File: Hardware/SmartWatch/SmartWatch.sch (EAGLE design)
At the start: 70 parts, among them U1 STM32L476, U3 UG-2828GDEDF11, U4 FAN5331SX, U5 APDS-9960, U6 MCP73831, U7 AP2112K-3.3TRG-1

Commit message: finished schematic!
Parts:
- added R19, R22: 10k, resistor:R-US_R0603
- added R21: 10K, resistor:R-US_R0603
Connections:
- removed net BT_IRQ: U2.P0.25
- removed net MOSI/DATA1: U3.D1/SDIN
- removed net PA10: U1PORTA.P10
- removed net PA13: U1PORTA.P13
- removed net PA5: U1PORTA.P5
- removed net PA6: U1PORTA.P6
- removed net PA7: U1PORTA.P7
- removed net PA8: U1PORTA.P8
- removed net PB0: U1PORTB.P0
- removed net PB1: U1PORTB.P1
- removed net PB13: U1PORTB.P13
- removed net PB14: U1PORTB.P14
- removed net PB2: U1PORTB.P2
- removed net PB8: U1PORTB.P8
- removed net PB9: U1PORTB.P9
- removed net PC10: U1PORTC.P10
- removed net PC12: U1PORTC.P12
- removed net PC4: U1PORTC.P4
- removed net PC8: U1PORTC.P8
- removed net PC9: U1PORTC.P9
- removed net SCK/DATA0: U3.D0/SCK
- new net BT_INT: U1PORTC.P4, U2.P0.25
- new net OLED_MOSI: U1PORTC.P12, U3.D1/SDIN
- new net OLED_SCK: U1PORTC.P10, U3.D0/SCK
- net 3.3V: now also R21.2
- net BTN_BACK: now also U1PORTA.P10
- net BTN_DN: now also U1PORTB.P0
- net BTN_SEL: now also U1PORTB.P1
- net BTN_UP: now also U1PORTB.P2
- net BT_MISO: now also U1PORTA.P6
- net BT_MOSI: now also U1PORTA.P7
- net BT_SCK: now also U1PORTA.P5
- net GND: now also R19.1, R22.1
- net G_INT: now also U1PORTC.P8
- net IMU_INT: now also U1PORTC.P9
- net IMU_NRESET: now also R22.2, U1PORTA.P8
- net OLED_CS: now also R19.2
- net OLED_DC: now also U1PORTB.P9
- net OLED_RES: now also U1PORTB.P8
- net SCL: now also U1PORTB.P13
- net SDA: now also U1PORTB.P14
- net STAT: now also R21.1, U1PORTA.P13
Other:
- moved on the sheet: R11, R12, R2

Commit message: started board layout
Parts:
- added JP1: (no value), SparkFun-Connectors:M02PTH
- C1, C10, C11, C14, C2, C3, C4, C5, C6, C7, C8, C9: device microbuilder:CAP_CERAMIC0603MINI -> resistor:C-EUC0603
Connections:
- removed net 3.3V: BTN_BACK.34, BTN_BOOT0.34, BTN_DN.34, BTN_NRST.34, BTN_SEL.34, BTN_UP.34, C10.2, C11.2, C12.1, C13.1, C18.1, C19.1, C20.1, C21.1, C22.1, C23.1, C24.1, C25.1, C26.1, C29.1, C3.2, C5.2, C7.1, C9.2, L1.1, R21.2, R3.2, R8.2, R9.2, U$39.VCC, U$41.VCC, U$5.NBOOT, U$5.VDD, U$5.VDDIO, U1G$4.VBAT, U1G$4.VDD, U1G$4.VDD/PF5, U1G$4.VDD/VUSB, U1G$4.VDD1, U1G$4.VDDA/VREF+, U3.VCI, U3.VDDIO, U4.SHDN, U4.VIN, U5.LEDA, U5.VDD, U7.VCC
- net +3V3: now also BTN_BACK.34, BTN_BOOT0.34, BTN_DN.34, BTN_NRST.34, BTN_SEL.34, BTN_UP.34, C10.2, C11.2, C12.1, C13.1, C18.1, C19.1, C20.1, C21.1, C22.1, C23.1, C24.1, C25.1, C26.1, C29.1, C3.2, C5.2, C7.1, C9.2, L1.1, R21.2, R3.2, R8.2, R9.2, U$39.VCC, U$41.VCC, U$5.NBOOT, U$5.VDD, U$5.VDDIO, U1G$4.VBAT, U1G$4.VDD, U1G$4.VDD/PF5, U1G$4.VDD/VUSB, U1G$4.VDD1, U1G$4.VDDA/VREF+, U3.VCI, U3.VDDIO, U4.SHDN, U4.VIN, U5.LEDA, U5.VDD, U7.VCC
- net GND: now also JP1.1
- net VBAT: now also JP1.2
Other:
- moved on the sheet: C1, C10, C11, C4, C5, C7, C8

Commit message: updated with ext programming port also eliminated some gnd loops and added text
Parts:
- added JP2: (no value), SparkFun-Connectors:M04NO_SILK_ALL_ROUND
- C10: value 1.0uF -> 1uF
- C2, C6: value 10uF/16V -> 10uF
- C22: value 0.1nF -> 0.1uF
- R13, R14, R15, R16, R17, R18, R20, R21, R7, R9: value 10K -> 10k
- R4: value 600K -> 600k
- R6: value 100K -> 100k
- RN1: value (none) -> 22
- renumbered U$16 to U10, U$39 to U9, U$41 to U8, U$5 to U11
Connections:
- removed net PA9: U1PORTA.P9
- removed net PC14: U1PORTC.P14
- new net SWCLK: JP2.4, U1PORTA.P14
- new net SWDIO: JP2.3, U1PORTA.P13
- net +3V3: now also JP2.1
- net GND: now also JP2.2
- net OSC32_IN: now also U1PORTC.P14; no longer U1PORTA.P14
- net STAT: now also U1PORTA.P9; no longer U1PORTA.P13

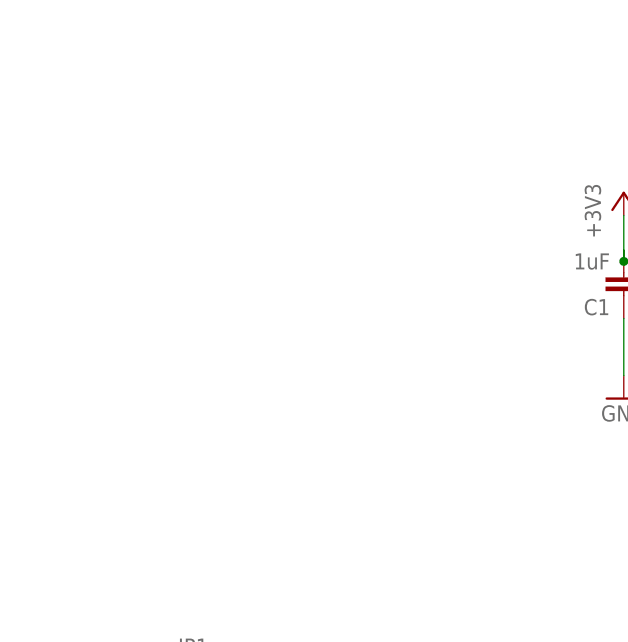
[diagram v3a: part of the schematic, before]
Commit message: added mounting holes
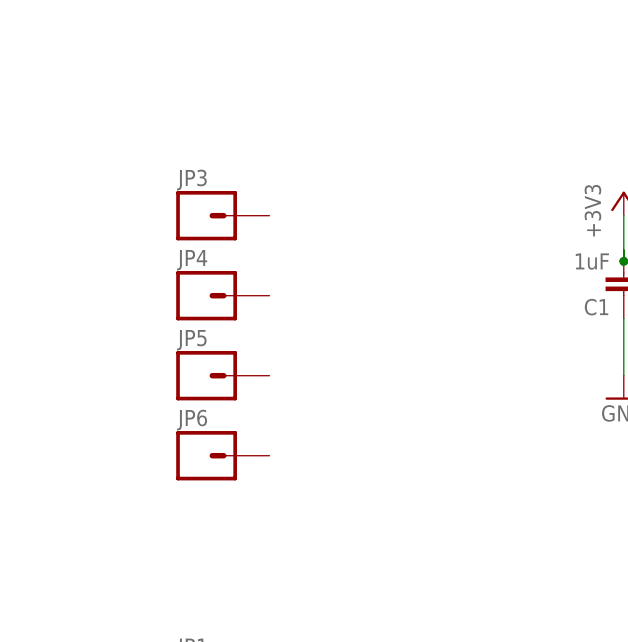
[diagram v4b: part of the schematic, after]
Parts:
- added JP3, JP4, JP5, JP6: (no value), SparkFun-Connectors:M01PTH_NO_SILK_YES_STOP
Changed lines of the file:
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@@
 <part name="JP1" library="SparkFun-Connectors" deviceset="M02" device="PTH"/>
 <part name="JP2" library="SparkFun-Connectors" deviceset="M04" device="NO_SILK_ALL_ROUND"/>
+<part name="JP3" library="SparkFun-Connectors" deviceset="M01" device="PTH_NO_SILK_YES_STOP"/>
+<part name="JP4" library="SparkFun-Connectors" deviceset="M01" device="PTH_NO_SILK_YES_STOP"/>
+<part name="JP5" library="SparkFun-Connectors" deviceset="M01" device="PTH_NO_SILK_YES_STOP"/>
+<part name="JP6" library="SparkFun-Connectors" deviceset="M01" device="PTH_NO_SILK_YES_STOP"/>
 </parts>
 <sheets>
@@
 <instance part="JP1" gate="G$1" x="-33.02" y="24.13"/>
 <instance part="JP2" gate="G$1" x="107.95" y="7.62"/>
+<instance part="JP3" gate="G$1" x="-33.02" y="78.74"/>
+<instance part="JP4" gate="G$1" x="-33.02" y="69.85"/>
+<instance part="JP5" gate="G$1" x="-33.02" y="60.96"/>
+<instance part="JP6" gate="G$1" x="-33.02" y="52.07"/>
 </instances>
 <busses>

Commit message: changed mounting holes to pin headers
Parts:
- JP1: device SparkFun-Connectors:M02PTH -> SparkFun-Connectors:M021X02_NO_SILK
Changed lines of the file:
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@@
 <part name="U$44" library="microbuilder" deviceset="3.3V" device=""/>
 <part name="R22" library="resistor" deviceset="R-US_" device="R0603" value="10k"/>
-<part name="JP1" library="SparkFun-Connectors" deviceset="M02" device="PTH"/>
+<part name="JP1" library="SparkFun-Connectors" deviceset="M02" device="1X02_NO_SILK"/>
 <part name="JP2" library="SparkFun-Connectors" deviceset="M04" device="NO_SILK_ALL_ROUND"/>
 <part name="JP3" library="SparkFun-Connectors" deviceset="M01" device="PTH_NO_SILK_YES_STOP"/>

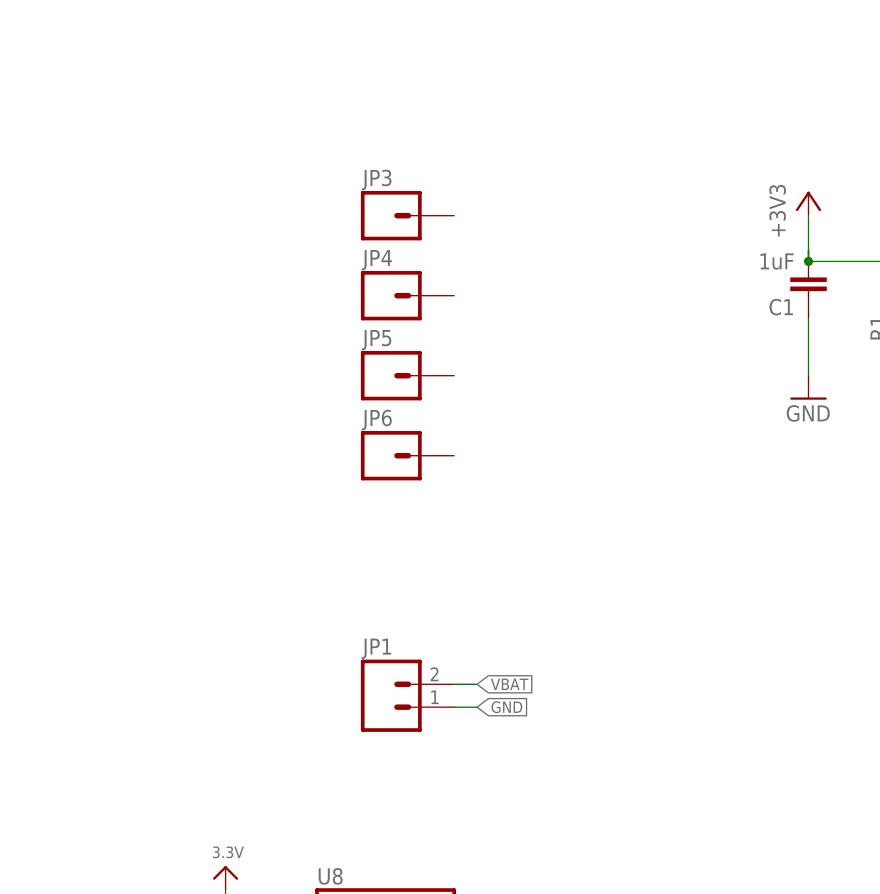
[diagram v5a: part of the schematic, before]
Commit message: added test points and icreased keepout around bluetooth
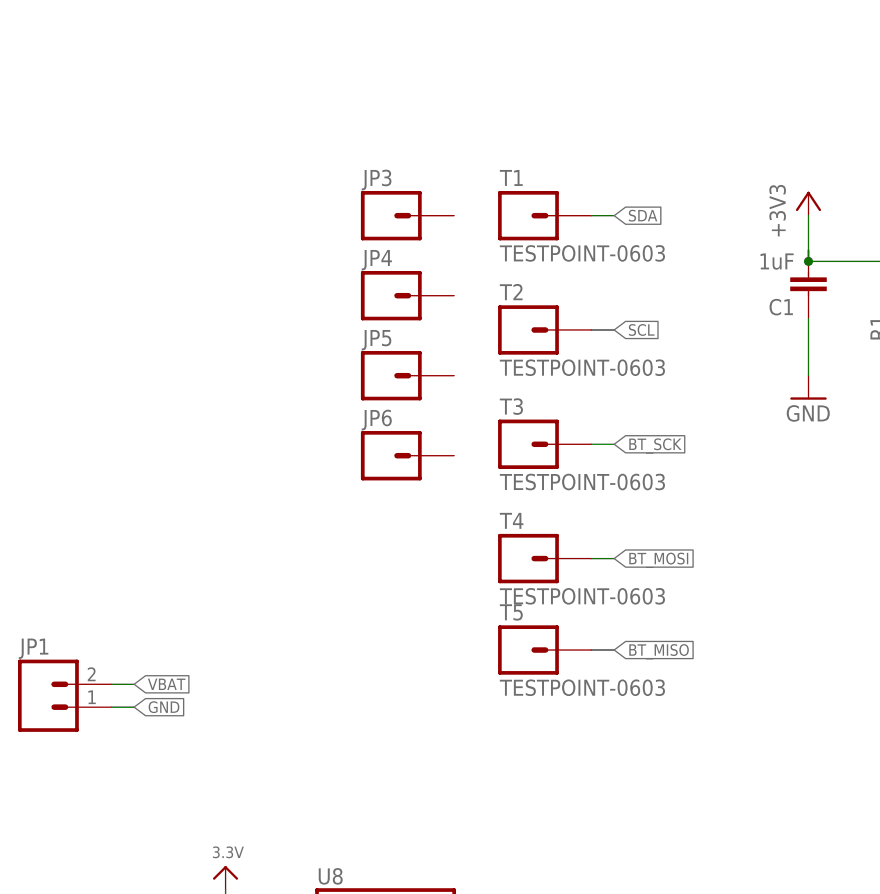
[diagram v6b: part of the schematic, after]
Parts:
- added T1, T2, T3, T4, T5: TESTPOINT-0603, SmartWatch:TESTPOINT-0603
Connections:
- net BT_MISO: now also T5.1
- net BT_MOSI: now also T4.1
- net BT_SCK: now also T3.1
- net SCL: now also T2.1
- net SDA: now also T1.1
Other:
- moved on the sheet: JP1
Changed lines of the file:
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@@
 <setting verticaltext="up"/>
 </settings>
-<grid distance="0.05" unitdist="inch" unit="inch" style="lines" multiple="1" display="yes" altdistance="0.005" altunitdist="inch" altunit="inch"/>
+<grid distance="0.1" unitdist="inch" unit="inch" style="lines" multiple="1" display="yes" altdistance="0.005" altunitdist="inch" altunit="inch"/>
 <layers>
 <layer number="1" name="Top" color="4" fill="1" visible="no" active="no"/>
@@
 <part name="JP5" library="SparkFun-Connectors" deviceset="M01" device="PTH_NO_SILK_YES_STOP"/>
 <part name="JP6" library="SparkFun-Connectors" deviceset="M01" device="PTH_NO_SILK_YES_STOP"/>
+<part name="T1" library="SmartWatch" deviceset="TESTPOINT-0603" device=""/>
+<part name="T2" library="SmartWatch" deviceset="TESTPOINT-0603" device=""/>
+<part name="T3" library="SmartWatch" deviceset="TESTPOINT-0603" device=""/>
+<part name="T4" library="SmartWatch" deviceset="TESTPOINT-0603" device=""/>
+<part name="T5" library="SmartWatch" deviceset="TESTPOINT-0603" device=""/>
 </parts>
 <sheets>
@@
 <instance part="U$44" gate="G$1" x="158.75" y="-8.89"/>
 <instance part="R22" gate="G$1" x="411.48" y="60.96" rot="R90"/>
-<instance part="JP1" gate="G$1" x="-33.02" y="24.13"/>
+<instance part="JP1" gate="G$1" x="-71.12" y="24.13"/>
 <instance part="JP2" gate="G$1" x="107.95" y="7.62"/>
 <instance part="JP3" gate="G$1" x="-33.02" y="78.74"/>
@@
 <instance part="JP5" gate="G$1" x="-33.02" y="60.96"/>
 <instance part="JP6" gate="G$1" x="-33.02" y="52.07"/>
+<instance part="T1" gate="G$1" x="-17.78" y="78.74"/>
+<instance part="T2" gate="G$1" x="-17.78" y="66.04"/>
+<instance part="T3" gate="G$1" x="-17.78" y="53.34"/>
+<instance part="T4" gate="G$1" x="-17.78" y="40.64"/>
+<instance part="T5" gate="G$1" x="-17.78" y="30.48"/>
 </instances>
 <busses>
@@
 <segment>
 <pinref part="JP1" gate="G$1" pin="1"/>
-<wire x1="-25.4" y1="24.13" x2="-22.86" y2="24.13" width="0.1524" layer="91"/>
-<label x="-22.86" y="24.13" size="1.27" layer="95" xref="yes"/>
+<wire x1="-63.5" y1="24.13" x2="-60.96" y2="24.13" width="0.1524" layer="91"/>
+<label x="-60.96" y="24.13" size="1.27" layer="95" xref="yes"/>
 </segment>
 <segment>
@@
 <label x="20.32" y="-15.24" size="1.27" layer="95" rot="R180" xref="yes"/>
 </segment>
+<segment>
+<pinref part="T3" gate="G$1" pin="1"/>
+<wire x1="-10.16" y1="53.34" x2="-7.62" y2="53.34" width="0.1524" layer="91"/>
+<label x="-7.62" y="53.34" size="1.27" layer="95" xref="yes"/>
+</segment>
 </net>
 <net name="BT_MISO" class="0">
@@
 <label x="20.32" y="-17.78" size="1.27" layer="95" rot="R180" xref="yes"/>
 </segment>
+<segment>
+<pinref part="T5" gate="G$1" pin="1"/>
+<wire x1="-10.16" y1="30.48" x2="-7.62" y2="30.48" width="0.1524" layer="91"/>
+<label x="-7.62" y="30.48" size="1.27" layer="95" xref="yes"/>
+</segment>
 </net>
 <net name="BT_MOSI" class="0">
@@
 <wire x1="22.86" y1="-20.32" x2="20.32" y2="-20.32" width="0.1524" layer="91"/>
 <label x="20.32" y="-20.32" size="1.27" layer="95" rot="R180" xref="yes"/>
+</segment>
+<segment>
+<pinref part="T4" gate="G$1" pin="1"/>
+<wire x1="-10.16" y1="40.64" x2="-7.62" y2="40.64" width="0.1524" layer="91"/>
+<label x="-7.62" y="40.64" size="1.27" layer="95" xref="yes"/>
 </segment>
 </net>
@@
 <label x="49.53" y="-38.1" size="1.27" layer="95" rot="R180" xref="yes"/>
 </segment>
+<segment>
+<pinref part="T1" gate="G$1" pin="1"/>
+<wire x1="-10.16" y1="78.74" x2="-7.62" y2="78.74" width="0.1524" layer="91"/>
+<label x="-7.62" y="78.74" size="1.27" layer="95" xref="yes"/>
+</segment>
 </net>
 <net name="SCL" class="0">
@@
 <wire x1="52.07" y1="-35.56" x2="49.53" y2="-35.56" width="0.1524" layer="91"/>
 <label x="49.53" y="-35.56" size="1.27" layer="95" rot="R180" xref="yes"/>
+</segment>
+<segment>
+<pinref part="T2" gate="G$1" pin="1"/>
+<wire x1="-10.16" y1="66.04" x2="-7.62" y2="66.04" width="0.1524" layer="91"/>
+<label x="-7.62" y="66.04" size="1.27" layer="95" xref="yes"/>
 </segment>
 </net>
@@
 <segment>
 <pinref part="JP1" gate="G$1" pin="2"/>
-<wire x1="-25.4" y1="26.67" x2="-22.86" y2="26.67" width="0.1524" layer="91"/>
-<label x="-22.86" y="26.67" size="1.27" layer="95" xref="yes"/>
-</segment>
-</net>
+<wire x1="-63.5" y1="26.67" x2="-60.96" y2="26.67" width="0.1524" layer="91"/>
+<label x="-60.96" y="26.67" size="1.27" layer="95" xref="yes"/>
+</segment>
+</net>

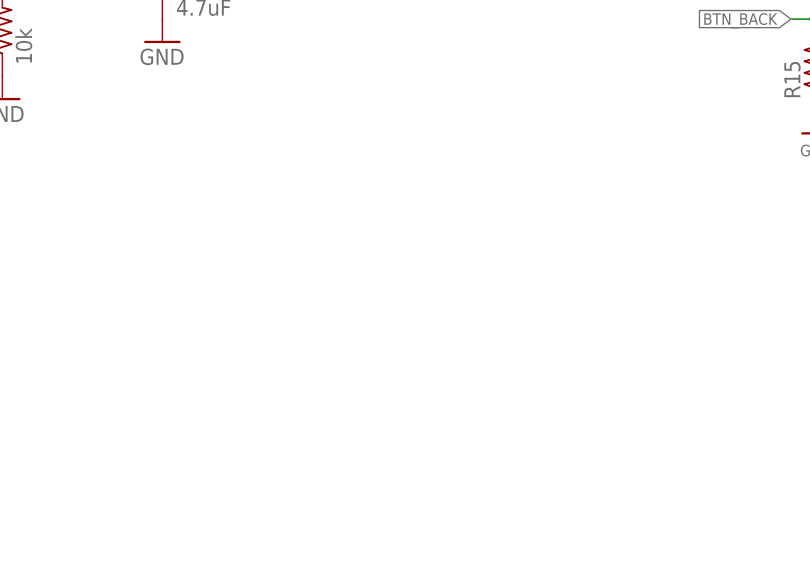
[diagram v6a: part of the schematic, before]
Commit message: added leds, need to figure out which pins they go to
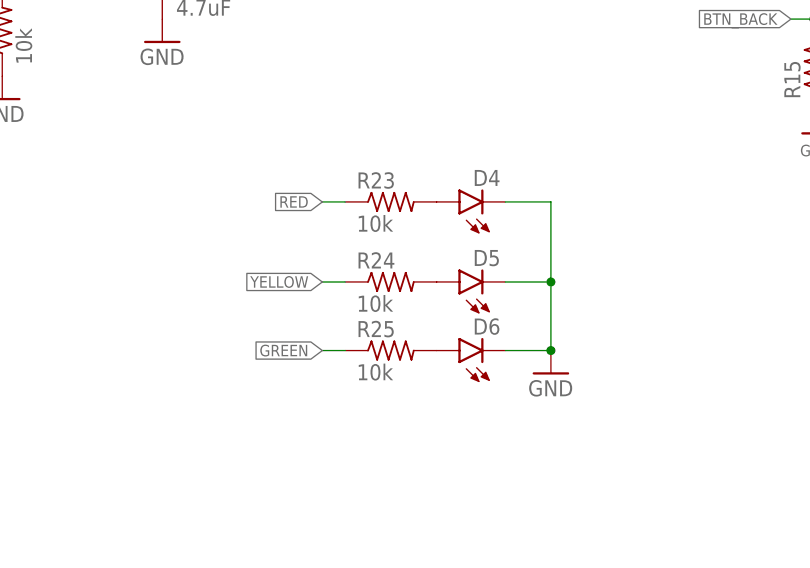
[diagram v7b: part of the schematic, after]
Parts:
- added D4, D5, D6: (no value), SparkFun-LED:LED0603
- added R23, R24, R25: 10k, resistor:R-US_R0603
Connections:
- new net GREEN: R25.1
- new net N$16: D4.A, R23.2
- new net N$18: D5.A, R24.2
- new net N$19: D6.A, R25.2
- new net RED: R23.1
- new net YELLOW: R24.1
- net GND: now also D4.C, D5.C, D6.C
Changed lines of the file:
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@@
 <setting verticaltext="up"/>
 </settings>
-<grid distance="0.1" unitdist="inch" unit="inch" style="lines" multiple="1" display="yes" altdistance="0.005" altunitdist="inch" altunit="inch"/>
+<grid distance="0.05" unitdist="inch" unit="inch" style="lines" multiple="1" display="yes" altdistance="0.005" altunitdist="inch" altunit="inch"/>
 <layers>
 <layer number="1" name="Top" color="4" fill="1" visible="no" active="no"/>
@@
 <part name="T4" library="SmartWatch" deviceset="TESTPOINT-0603" device=""/>
 <part name="T5" library="SmartWatch" deviceset="TESTPOINT-0603" device=""/>
+<part name="D4" library="SparkFun-LED" deviceset="LED" device="0603"/>
+<part name="D5" library="SparkFun-LED" deviceset="LED" device="0603"/>
+<part name="D6" library="SparkFun-LED" deviceset="LED" device="0603"/>
+<part name="GND16" library="SparkFun" deviceset="GND" device=""/>
+<part name="R23" library="resistor" deviceset="R-US_" device="R0603" value="10k"/>
+<part name="R24" library="resistor" deviceset="R-US_" device="R0603" value="10k"/>
+<part name="R25" library="resistor" deviceset="R-US_" device="R0603" value="10k"/>
 </parts>
 <sheets>
@@
 <instance part="T4" gate="G$1" x="-17.78" y="40.64"/>
 <instance part="T5" gate="G$1" x="-17.78" y="30.48"/>
+<instance part="D4" gate="G$1" x="251.46" y="-62.23" rot="R90"/>
+<instance part="D5" gate="G$1" x="251.46" y="-71.12" rot="R90"/>
+<instance part="D6" gate="G$1" x="251.46" y="-78.74" rot="R90"/>
+<instance part="GND16" gate="1" x="261.62" y="-81.28"/>
+<instance part="R23" gate="G$1" x="243.84" y="-62.23"/>
+<instance part="R24" gate="G$1" x="243.84" y="-71.12"/>
+<instance part="R25" gate="G$1" x="243.84" y="-78.74"/>
 </instances>
 <busses>
@@
 <label x="115.57" y="7.62" size="1.27" layer="95" xref="yes"/>
 </segment>
+<segment>
+<pinref part="D4" gate="G$1" pin="C"/>
+<pinref part="GND16" gate="1" pin="GND"/>
+<wire x1="256.54" y1="-62.23" x2="261.62" y2="-62.23" width="0.1524" layer="91"/>
+<wire x1="261.62" y1="-62.23" x2="261.62" y2="-71.12" width="0.1524" layer="91"/>
+<pinref part="D5" gate="G$1" pin="C"/>
+<wire x1="261.62" y1="-71.12" x2="261.62" y2="-78.74" width="0.1524" layer="91"/>
+<wire x1="256.54" y1="-71.12" x2="261.62" y2="-71.12" width="0.1524" layer="91"/>
+<junction x="261.62" y="-71.12"/>
+<pinref part="D6" gate="G$1" pin="C"/>
+<wire x1="256.54" y1="-78.74" x2="261.62" y2="-78.74" width="0.1524" layer="91"/>
+<junction x="261.62" y="-78.74"/>
+</segment>
 </net>
 <net name="BT_SCK" class="0">
@@
 </segment>
 </net>
+<net name="N$16" class="0">
+<segment>
+<pinref part="D4" gate="G$1" pin="A"/>
+<pinref part="R23" gate="G$1" pin="2"/>
+</segment>
+</net>
+<net name="N$18" class="0">
+<segment>
+<pinref part="D5" gate="G$1" pin="A"/>
+<pinref part="R24" gate="G$1" pin="2"/>
+</segment>
+</net>
+<net name="N$19" class="0">
+<segment>
+<pinref part="D6" gate="G$1" pin="A"/>
+<pinref part="R25" gate="G$1" pin="2"/>
+</segment>
+</net>
+<net name="RED" class="0">
+<segment>
+<pinref part="R23" gate="G$1" pin="1"/>
+<wire x1="238.76" y1="-62.23" x2="236.22" y2="-62.23" width="0.1524" layer="91"/>
+<label x="236.22" y="-62.23" size="1.27" layer="95" rot="R180" xref="yes"/>
+</segment>
+</net>
+<net name="YELLOW" class="0">
+<segment>
+<pinref part="R24" gate="G$1" pin="1"/>
+<wire x1="238.76" y1="-71.12" x2="236.22" y2="-71.12" width="0.1524" layer="91"/>
+<label x="236.22" y="-71.12" size="1.27" layer="95" rot="R180" xref="yes"/>
+</segment>
+</net>
+<net name="GREEN" class="0">
+<segment>
+<pinref part="R25" gate="G$1" pin="1"/>
+<wire x1="238.76" y1="-78.74" x2="236.22" y2="-78.74" width="0.1524" layer="91"/>
+<label x="236.22" y="-78.74" size="1.27" layer="95" rot="R180" xref="yes"/>
+</segment>
+</net>

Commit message: finished schematic
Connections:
- removed net PB3: U1PORTB.P3
- removed net PB4: U1PORTB.P4
- removed net PB5: U1PORTB.P5
- net GREEN: now also U1PORTB.P5
- net RED: now also U1PORTB.P3
- net YELLOW: now also U1PORTB.P4
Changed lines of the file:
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@@
 <setting verticaltext="up"/>
 </settings>
-<grid distance="0.05" unitdist="inch" unit="inch" style="lines" multiple="1" display="yes" altdistance="0.005" altunitdist="inch" altunit="inch"/>
+<grid distance="0.1" unitdist="inch" unit="inch" style="lines" multiple="1" display="no" altdistance="0.01" altunitdist="inch" altunit="inch"/>
 <layers>
 <layer number="1" name="Top" color="4" fill="1" visible="no" active="no"/>
@@
 </segment>
 </net>
-<net name="PB3" class="0">
-<segment>
-<pinref part="U1" gate="PORTB" pin="P3"/>
-<wire x1="52.07" y1="-10.16" x2="49.53" y2="-10.16" width="0.1524" layer="91"/>
-<label x="49.53" y="-10.16" size="1.27" layer="95" rot="R180" xref="yes"/>
-</segment>
-</net>
-<net name="PB4" class="0">
-<segment>
-<pinref part="U1" gate="PORTB" pin="P4"/>
-<wire x1="52.07" y1="-12.7" x2="49.53" y2="-12.7" width="0.1524" layer="91"/>
-<label x="49.53" y="-12.7" size="1.27" layer="95" rot="R180" xref="yes"/>
-</segment>
-</net>
-<net name="PB5" class="0">
-<segment>
-<pinref part="U1" gate="PORTB" pin="P5"/>
-<wire x1="52.07" y1="-15.24" x2="49.53" y2="-15.24" width="0.1524" layer="91"/>
-<label x="49.53" y="-15.24" size="1.27" layer="95" rot="R180" xref="yes"/>
-</segment>
-</net>
 <net name="PB6" class="0">
 <segment>
@@
 <label x="236.22" y="-62.23" size="1.27" layer="95" rot="R180" xref="yes"/>
 </segment>
+<segment>
+<pinref part="U1" gate="PORTB" pin="P3"/>
+<wire x1="52.07" y1="-10.16" x2="49.53" y2="-10.16" width="0.1524" layer="91"/>
+<label x="49.53" y="-10.16" size="1.27" layer="95" rot="R180" xref="yes"/>
+</segment>
 </net>
 <net name="YELLOW" class="0">
@@
 <label x="236.22" y="-71.12" size="1.27" layer="95" rot="R180" xref="yes"/>
 </segment>
+<segment>
+<pinref part="U1" gate="PORTB" pin="P4"/>
+<wire x1="52.07" y1="-12.7" x2="49.53" y2="-12.7" width="0.1524" layer="91"/>
+<label x="49.53" y="-12.7" size="1.27" layer="95" rot="R180" xref="yes"/>
+</segment>
 </net>
 <net name="GREEN" class="0">
@@
 <label x="236.22" y="-78.74" size="1.27" layer="95" rot="R180" xref="yes"/>
 </segment>
-</net>
+<segment>
+<pinref part="U1" gate="PORTB" pin="P5"/>
+<wire x1="52.07" y1="-15.24" x2="49.53" y2="-15.24" width="0.1524" layer="91"/>
+<label x="49.53" y="-15.24" size="1.27" layer="95" rot="R180" xref="yes"/>
+</segment>
+</net>
